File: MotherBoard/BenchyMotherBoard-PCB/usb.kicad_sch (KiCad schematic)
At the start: 92 parts, among them J10 USB3_B, J11 USB3-PORT2, J12 USB3-PORT3, J13 USB3-PORT4, J14 USB3-PORT5, J15 USB-INTERNAL-PORT1, J16 TFT-DISPLAY, J17 USB-INTERNAL-PORT2, J9 USB3-PORT1, Q3 RQ5A030AP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

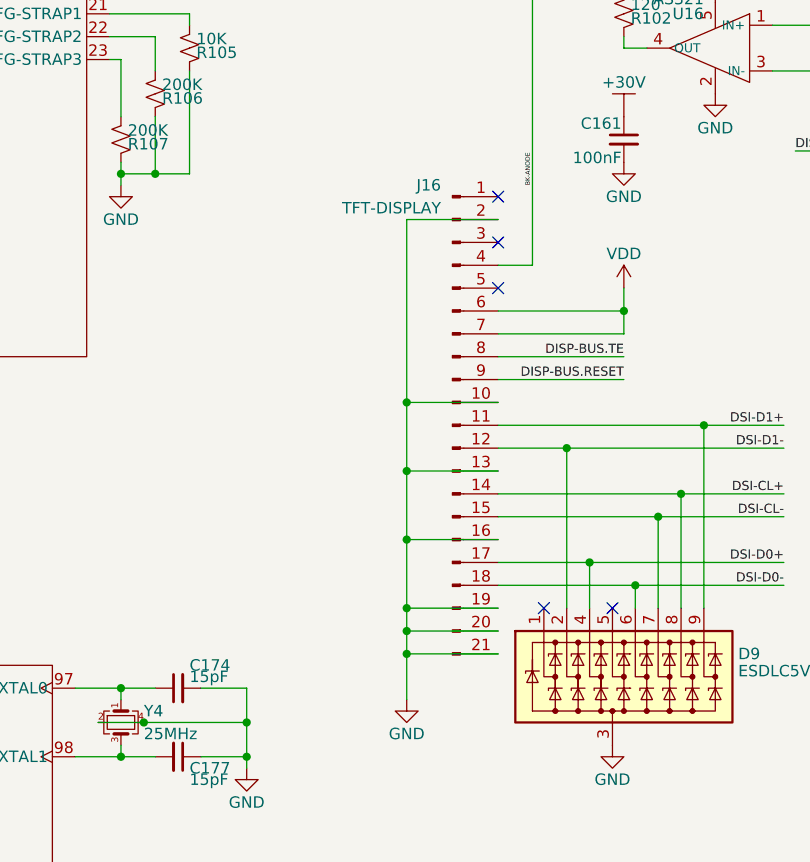
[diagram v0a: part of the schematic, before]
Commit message: Initial DDR routing, start fixing skew
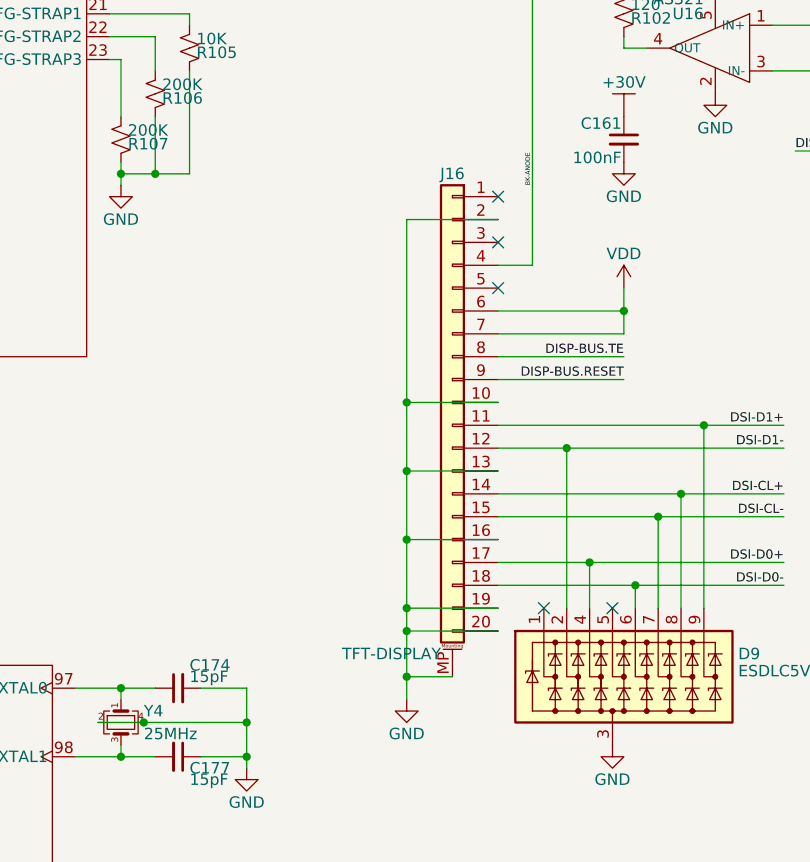
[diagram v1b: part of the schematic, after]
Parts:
- removed J16: TFT-DISPLAY, Daxxn_Connectors:FH12A-20S-0.5SH55, symbol Connector:Conn_01x21_Male
- added J16: TFT-DISPLAY, Daxxn_Connectors:FH12A-20S-0.5SH55, symbol Connector_Generic_MountingPin:Conn_01x20_MountingPin
- D1, D2, D3, D4, D5, D9: footprint Daxxn_Packages:U-DFN3810-9 -> Package_DFN_QFN:UDFN-9_1.0x3.8mm_P0.5mm
- U1: footprint Daxxn_Packages:LFBGA354-P0.8mm -> Daxxn_Packages:LFBGA354-P0.8mm-STM32MP157F
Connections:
- net BK-ANODE: now also J16.4 (Pin_4)
- net DISP-BUS.RESET: now also J16.9 (Pin_9)
- net DISP-BUS.TE: now also J16.8 (Pin_8)
- net DSI-CL+: now also J16.14 (Pin_14)
- net DSI-CL-: now also J16.15 (Pin_15)
- net DSI-D0+: now also J16.17 (Pin_17)
- net DSI-D0-: now also J16.18 (Pin_18)
- net DSI-D1+: now also J16.11 (Pin_11)
- net DSI-D1-: now also J16.12 (Pin_12)
- net GND: now also J16.10 (Pin_10), J16.13 (Pin_13), J16.16 (Pin_16), J16.19 (Pin_19), J16.2 (Pin_2), J16.20 (Pin_20), J16.MP (MountPin)
- net VDD: now also J16.6 (Pin_6), J16.7 (Pin_7)
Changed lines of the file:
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@@
   (junction (at 375.92 69.85) (diameter 0) (color 0 0 0 0)
   )
-  (junction (at 140.97 241.3) (diameter 0) (color 0 0 0 0)
-  )
   (junction (at 50.8 190.5) (diameter 0) (color 0 0 0 0)
   )
@@
   (junction (at 270.51 71.12) (diameter 0) (color 0 0 0 0)
   )
+  (junction (at 140.97 243.84) (diameter 0) (color 0 0 0 0)
+  )
   (junction (at 50.8 201.93) (diameter 0) (color 0 0 0 0)
   )
@@
     (stroke (width 0) (type default))
   )
-  (wire (pts (xy 140.97 241.3) (xy 140.97 246.38))
+  (wire (pts (xy 140.97 238.76) (xy 140.97 243.84))
     (stroke (width 0) (type default))
   )
@@
     (stroke (width 0) (type default))
   )
+  (wire (pts (xy 140.97 243.84) (xy 140.97 246.38))
+    (stroke (width 0) (type default))
+  )
   (wire (pts (xy 148.59 33.02) (xy 157.48 33.02))
     (stroke (width 0) (type default))
@@
     (stroke (width 0) (type default))
   )
-  (wire (pts (xy 140.97 238.76) (xy 140.97 241.3))
-    (stroke (width 0) (type default))
-  )
   (wire (pts (xy 299.72 215.9) (xy 302.26 218.44))
     (stroke (width 0) (type default))
@@
     (stroke (width 0) (type default))
   )
-  (wire (pts (xy 140.97 241.3) (xy 151.13 241.3))
-    (stroke (width 0) (type default))
-  )
   (wire (pts (xy 243.84 20.32) (xy 246.38 20.32))
     (stroke (width 0) (type default))
@@
     (stroke (width 0) (type default))
   )
+  (wire (pts (xy 140.97 243.84) (xy 146.05 243.84))
+    (stroke (width 0) (type default))
+  )
   (bus (pts (xy 207.01 271.78) (xy 207.01 276.86))
     (stroke (width 0) (type default))
@@
       (effects (font (size 1.27 1.27)) (justify left))
     )
-    (property "Footprint" "Daxxn_Packages:U-DFN3810-9" (at 384.81 128.27 0)
+    (property "Footprint" "Package_DFN_QFN:UDFN-9_1.0x3.8mm_P0.5mm" (at 384.81 128.27 0)
       (effects (font (size 1.27 1.27)) (justify left) hide)
     )
@@
       (effects (font (size 1.27 1.27)) (justify left))
     )
-    (property "Footprint" "Daxxn_Packages:U-DFN3810-9" (at 289.56 99.06 0)
+    (property "Footprint" "Package_DFN_QFN:UDFN-9_1.0x3.8mm_P0.5mm" (at 289.56 99.06 0)
       (effects (font (size 1.27 1.27)) (justify left) hide)
     )
@@
       (effects (font (size 1.27 1.27)) (justify left))
     )
-    (property "Footprint" "Daxxn_Packages:LFBGA354-P0.8mm" (at 213.36 187.96 0)
+    (property "Footprint" "Daxxn_Packages:LFBGA354-P0.8mm-STM32MP157F" (at 213.36 187.96 0)
       (effects (font (size 1.27 1.27)) (justify left) hide)
     )
@@
       (effects (font (size 1.27 1.27)) (justify left))
     )
-    (property "Footprint" "Daxxn_Packages:U-DFN3810-9" (at 289.56 144.78 0)
+    (property "Footprint" "Package_DFN_QFN:UDFN-9_1.0x3.8mm_P0.5mm" (at 289.56 144.78 0)
       (effects (font (size 1.27 1.27)) (justify left) hide)
     )
@@
       (effects (font (size 1.27 1.27)) (justify left))
     )
-    (property "Footprint" "Daxxn_Packages:U-DFN3810-9" (at 177.8 245.11 0)
+    (property "Footprint" "Package_DFN_QFN:UDFN-9_1.0x3.8mm_P0.5mm" (at 177.8 245.11 0)
       (effects (font (size 1.27 1.27)) (justify left) hide)
     )
@@
       (effects (font (size 1.27 1.27)) (justify left))
     )
-    (property "Footprint" "Daxxn_Packages:U-DFN3810-9" (at 384.81 82.55 0)
+    (property "Footprint" "Package_DFN_QFN:UDFN-9_1.0x3.8mm_P0.5mm" (at 384.81 82.55 0)
       (effects (font (size 1.27 1.27)) (justify left) hide)
     )
@@
     )
   )
-  (symbol (lib_id "power:GND") (at 275.59 59.69 0) (unit 1)
+  (symbol (lib_id "Connector_Generic_MountingPin:Conn_01x20_MountingPin") (at 146.05 213.36 0) (mirror y) (unit 1)
     (in_bom yes) (on_board yes) (dnp no)
-    (property "Reference" "#PWR0129" (at 275.59 66.04 0)
+    (property "Reference" "J16" (at 146.05 187.96 0)
+      (effects (font (size 1.27 1.27)))
+    )
+    (property "Value" "TFT-DISPLAY" (at 144.78 241.3 0)
+      (effects (font (size 1.27 1.27)) (justify left))
+    )
+    (property "Footprint" "Daxxn_Connectors:FH12A-20S-0.5SH55" (at 146.05 213.36 0)
       (effects (font (size 1.27 1.27)) hide)
     )
-    (property "Value" "GND" (at 275.59 63.5 0)
-      (effects (font (size 1.27 1.27)))
+    (property "Datasheet" "~" (at 146.05 213.36 0)
+      (effects (font (size 1.27 1.27)) hide)
     )
-    (property "Footprint" "" (at 275.59 59.69 0)
+    (property "Schematic" "" (at 146.05 213.36 0)
       (effects (font (size 1.27 1.27)) hide)
     )
-    (property "Datasheet" "" (at 275.59 59.69 0)
+    (property "PartNumber" "" (at 146.05 213.36 0)
+      (effects (font (size 1.27 1.27)))
+    )
+    (property "SupplierPN" "" (at 146.05 213.36 0)
       (effects (font (size 1.27 1.27)) hide)
     )
     (pin "1")
+    (pin "10")
+    (pin "11")
+    (pin "12")
+    (pin "13")
+    (pin "14")
+    (pin "15")
+    (pin "16")
+    (pin "17")
+    (pin "18")
+    (pin "19")
+    (pin "2")
+    (pin "20")
+    (pin "3")
+    (pin "4")
+    (pin "5")
+    (pin "6")
+    (pin "7")
+    (pin "8")
+    (pin "9")
+    (pin "MP")
     (instances
       (project "BenchyMotherBoard-PCB"
         (path "/2ea077fe-b0e6-467f-a1c1-8336ebdb7a86/68580c3e-f594-4791-9d78-5a4c0a75f436"
-          (reference "#PWR0129") (unit 1)
+          (reference "J16") (unit 1)
         )
       )
     )
   )
-  (symbol (lib_id "Connector:USB3_B") (at 27.94 43.18 0) (unit 1)
+  (symbol (lib_id "power:GND") (at 275.59 59.69 0) (unit 1)
     (in_bom yes) (on_board yes) (dnp no)
-    (property "Reference" "J10" (at 17.78 27.94 0)
-      (effects (font (size 1.27 1.27)) (justify left))
+    (property "Reference" "#PWR0129" (at 275.59 66.04 0)
+      (effects (font (size 1.27 1.27)) hide)
     )
-    (property "Value" "USB3_B" (at 38.1 27.94 0)
-      (effects (font (size 1.27 1.27)) (justify right))
+    (property "Value" "GND" (at 275.59 63.5 0)
+      (effects (font (size 1.27 1.27)))
     )
-    (property "Footprint" "Daxxn_Connectors:USB-GSB3211311WEU" (at 31.75 40.64 0)
+    (property "Footprint" "" (at 275.59 59.69 0)
       (effects (font (size 1.27 1.27)) hide)
     )
-    (property "Datasheet" "~" (at 31.75 40.64 0)
+    (property "Datasheet" "" (at 275.59 59.69 0)
       (effects (font (size 1.27 1.27)) hide)
     )
     (pin "1")
-    (pin "10")
-    (pin "2")
-    (pin "3")
-    (pin "4")
-    (pin "5")
-    (pin "6")
-    (pin "7")
-    (pin "8")
-    (pin "9")
     (instances
       (project "BenchyMotherBoard-PCB"
         (path "/2ea077fe-b0e6-467f-a1c1-8336ebdb7a86/68580c3e-f594-4791-9d78-5a4c0a75f436"
-          (reference "J10") (unit 1)
+          (reference "#PWR0129") (unit 1)
         )
       )
     )
   )
-  (symbol (lib_id "Connector:Conn_01x21_Male") (at 146.05 215.9 0) (unit 1)
+  (symbol (lib_id "Connector:USB3_B") (at 27.94 43.18 0) (unit 1)
     (in_bom yes) (on_board yes) (dnp no)
-    (property "Reference" "J16" (at 144.78 189.23 0)
-      (effects (font (size 1.27 1.27)) (justify right))
+    (property "Reference" "J10" (at 17.78 27.94 0)
+      (effects (font (size 1.27 1.27)) (justify left))
     )
-    (property "Value" "TFT-DISPLAY" (at 144.78 191.77 0)
+    (property "Value" "USB3_B" (at 38.1 27.94 0)
       (effects (font (size 1.27 1.27)) (justify right))
     )
-    (property "Footprint" "Daxxn_Connectors:FH12A-20S-0.5SH55" (at 146.05 215.9 0)
+    (property "Footprint" "Daxxn_Connectors:USB-GSB3211311WEU" (at 31.75 40.64 0)
       (effects (font (size 1.27 1.27)) hide)
     )
-    (property "Datasheet" "~" (at 146.05 215.9 0)
+    (property "Datasheet" "~" (at 31.75 40.64 0)
       (effects (font (size 1.27 1.27)) hide)
     )
     (pin "1")
     (pin "10")
-    (pin "11")
-    (pin "12")
-    (pin "13")
-    (pin "14")
-    (pin "15")
-    (pin "16")
-    (pin "17")
-    (pin "18")
-    (pin "19")
     (pin "2")
-    (pin "20")
-    (pin "21")
     (pin "3")
     (pin "4")
@@
       (project "BenchyMotherBoard-PCB"
         (path "/2ea077fe-b0e6-467f-a1c1-8336ebdb7a86/68580c3e-f594-4791-9d78-5a4c0a75f436"
-          (reference "J16") (unit 1)
+          (reference "J10") (unit 1)
         )
       )
@@
       (effects (font (size 1.27 1.27)) (justify left))
     )
-    (property "Footprint" "Daxxn_Packages:U-DFN3810-9" (at 289.56 53.34 0)
+    (property "Footprint" "Package_DFN_QFN:UDFN-9_1.0x3.8mm_P0.5mm" (at 289.56 53.34 0)
       (effects (font (size 1.27 1.27)) (justify left) hide)
     )
